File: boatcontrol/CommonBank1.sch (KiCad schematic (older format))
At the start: 24 parts, among them J201 Conn_01x01_Male, J202 Conn_01x01_Male, J203 TBP01R2W-508-16BE, J204 Conn_01x01_Male, J205 Conn_01x01_Male, J206 TBL008V-1000-02BE, Q203 IPP120P04P4L-03, U201 MCP23017-E/SP, U202 MCP23017-E/SP

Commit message: RPi scheme update done
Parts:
- JP209: value Jumper_NO_Small -> Jumper_NC_Small; symbol Device:Jumper_NO_Small -> Device:Jumper_NC_Small
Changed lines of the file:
@@
 	8500 5550 8500 5750
 $Comp
-L Device:Jumper_NO_Small JP?
+L Device:Jumper_NC_Small JP?
 U 1 1 617F409D
 P 9800 5800
@@
 AR Path="/D1BB8DB4/617F409D" Ref="JP?"  Part="1"
 F 0 "JP209" H 9800 5900 50  0000 C CNN
-F 1 "Jumper_NO_Small" H 9850 5700 50  0001 C CNN
+F 1 "Jumper_NC_Small" H 9850 5700 50  0001 C CNN
 F 2 "Connector_PinHeader_2.54mm:PinHeader_1x02_P2.54mm_Vertical" H 9800 5800 50  0001 C CNN
 F 3 "~" H 9800 5800 50  0001 C CNN

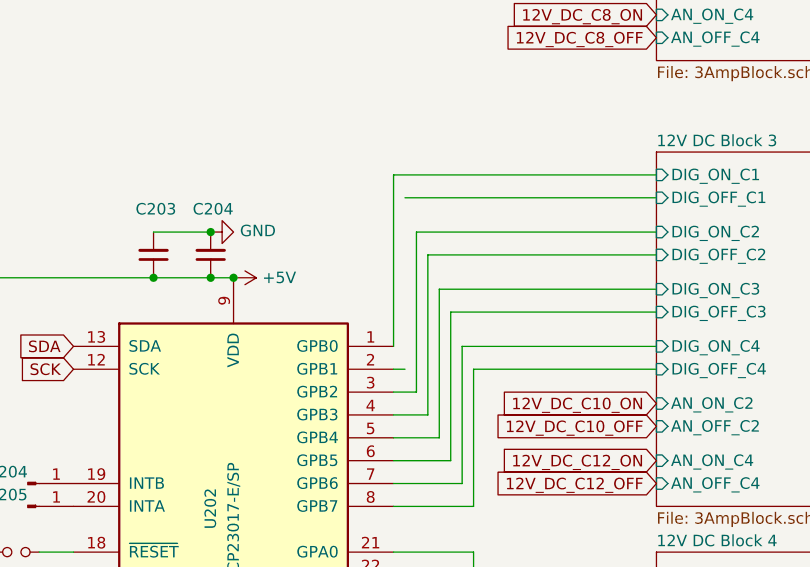
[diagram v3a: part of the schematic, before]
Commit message: Line up jumpers
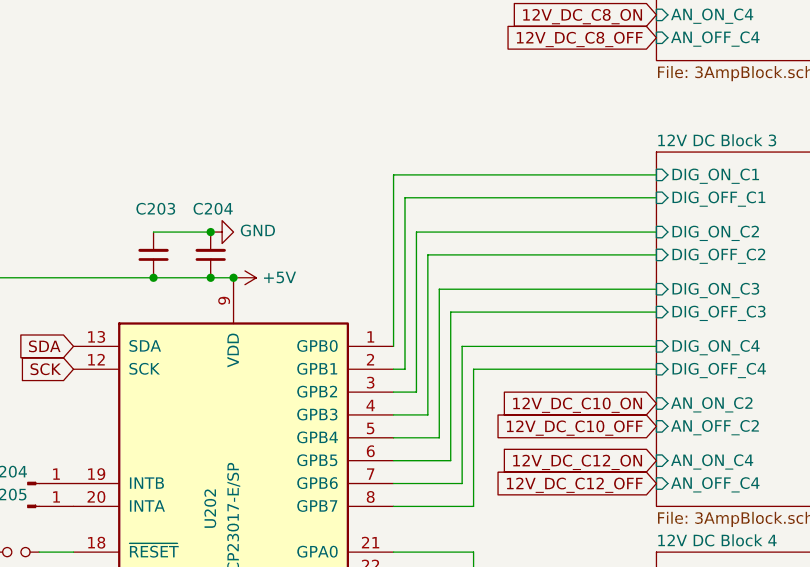
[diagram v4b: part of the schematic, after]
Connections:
- net 12V DC Block 3/DIG_OFF_C1: now also U202.2 (GPB1)
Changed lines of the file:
@@
 	-1   0    0    1
 $EndComp
+Wire Wire Line
+	4300 5350 4300 4600
 $EndSCHEMATC

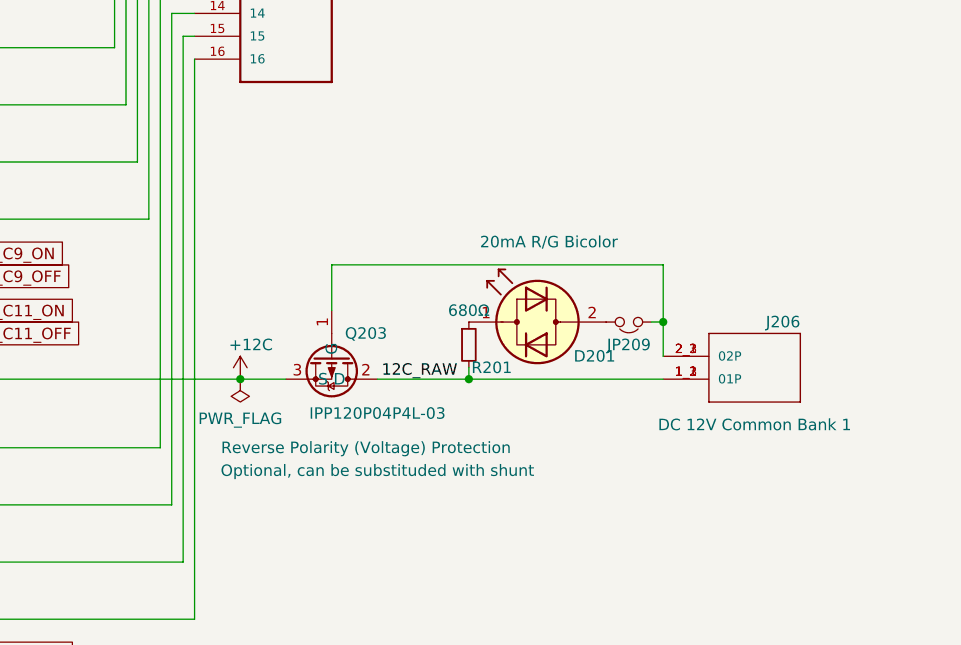
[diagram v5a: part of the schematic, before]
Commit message: Scale reverse polarity protection
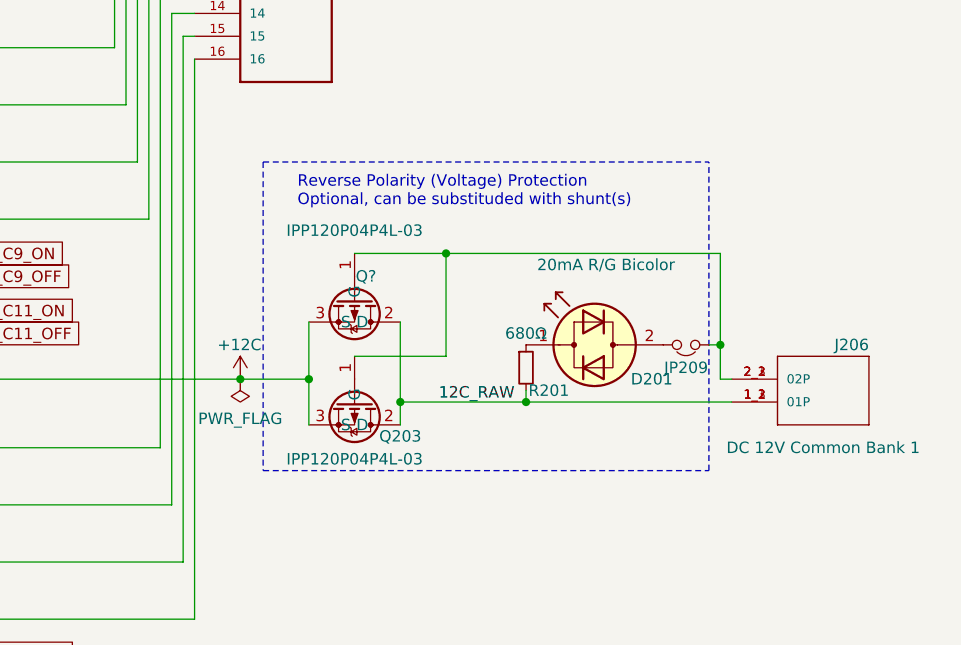
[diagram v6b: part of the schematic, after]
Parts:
- added Q?: IPP120P04P4L-03, Package_TO_SOT_THT:TO-220-3_Vertical, symbol BoatControl:IPP120P04P4L-03
- Q203: Field8 Optional, can be substituded with shunt -> (none); Purpose Reverse Polarity (Voltage) Protection -> (none)
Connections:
- net +12C: now also Q?.3 (S)
- net 12C_RAW: now also Q?.2 (D)
- net at J206.2_1 (02P), J206.2_2 (02P), J206.2_3 (02P)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: now also Q?.1 (G)
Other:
- note added: "Reverse Polarity (Voltage) Protection\nOptional, can be substituded with shunt(s)"
- moved on the sheet: D201, J206, JP209, Q203, R201
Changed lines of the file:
@@
 AR Path="/D1BB8DB4/D1AAA2AE" Ref="#PWR?"  Part="1"
 F 0 "#PWR0205" H 8100 5900 50  0001 C CNN
-F 1 "+12C" H 8050 6200 50  0000 L CNN
+F 1 "+12C" H 8000 6200 50  0000 L CNN
 F 2 "" H 8100 6050 50  0001 C CNN
 F 3 "" H 8100 6050 50  0001 C CNN
@@
 Wire Wire Line
 	6750 5250 6750 6050
-Wire Wire Line
-	8300 6050 8100 6050
 Connection ~ 6750 6050
 Wire Wire Line
@@
 Wire Wire Line
 	4600 1650 5400 1650
-Text Label 9050 6050 2    50   ~ 0
+Text Label 9300 6150 2    50   ~ 0
 12C_RAW
 Connection ~ 8100 6050
@@
 L BoatControl:TBL008V-1000-02BE J?
 U 1 1 D1AAA18D
-P 10350 5950
+P 10650 6050
 AR Path="/D1AAA18D" Ref="J?"  Part="1"
 AR Path="/D16552B4/D1AAA18D" Ref="J206"  Part="1"
 AR Path="/D1BB8DB4/D1AAA18D" Ref="J?"  Part="1"
-F 0 "J206" H 10550 5800 50  0000 R CNN
-F 1 "TBL008V-1000-02BE" H 10700 5800 50  0001 R CNN
-F 2 "CUI_TBL008V-1000-02BE" H 10350 5950 50  0001 L BNN
-F 3 "CUI" H 10350 5950 50  0001 L BNN
-F 4 "DC 12V Common Bank 1" H 10350 6250 50  0000 C CNN "Type"
-	1    10350 5950
+F 0 "J206" H 10850 5900 50  0000 R CNN
+F 1 "TBL008V-1000-02BE" H 11000 5900 50  0001 R CNN
+F 2 "CUI_TBL008V-1000-02BE" H 10650 6050 50  0001 L BNN
+F 3 "CUI" H 10650 6050 50  0001 L BNN
+F 4 "DC 12V Common Bank 1" H 10650 6350 50  0000 C CNN "Type"
+	1    10650 6050
 	1    0    0    1
 $EndComp
@@
 L BoatControl:IPP120P04P4L-03 Q203
 U 1 1 5FEBFE7C
-P 8500 6050
-F 0 "Q203" V 8300 6200 50  0000 C CNN
-F 1 "IPP120P04P4L-03" V 8650 6250 50  0000 C CNN
-F 2 "Package_TO_SOT_THT:TO-220-3_Vertical" H 8150 6600 50  0001 C CNN
-F 3 "https://www.infineon.com/dgdl/Infineon-I80P03P4L_04-DS-v01_01-en.pdf?folderId=db3a304314dca3890114ef902baa05f9&fileId=db3a30431ddc9372011e07e95eb827d7&ack=t" H 8500 6050 50  0001 C CNN
-F 4 "P-Channel 30V 80A (Tc) 137W (Tc) Through Hole PG-TO220-3-1" H 8350 6700 50  0001 C CNN "Description"
-F 5 "OptiMOS" H 9100 6350 50  0001 C CNN "Series"
-F 6 "Infineon Technologies" H 9000 6450 50  0001 C CNN "Infineon Technologies"
-F 7 "Reverse Polarity (Voltage) Protection" V 8800 6200 50  0000 C CNN "Purpose"
-F 8 "Optional, can be substituded with shunt" V 8900 6250 50  0000 C CNN "Field8"
-	1    8500 6050
+P 8600 6250
+F 0 "Q203" V 8650 6450 50  0000 C CNN
+F 1 "IPP120P04P4L-03" V 8750 6250 50  0000 C CNN
+F 2 "Package_TO_SOT_THT:TO-220-3_Vertical" H 8250 6800 50  0001 C CNN
+F 3 "https://www.infineon.com/dgdl/Infineon-I80P03P4L_04-DS-v01_01-en.pdf?folderId=db3a304314dca3890114ef902baa05f9&fileId=db3a30431ddc9372011e07e95eb827d7&ack=t" H 8600 6250 50  0001 C CNN
+F 4 "P-Channel 30V 80A (Tc) 137W (Tc) Through Hole PG-TO220-3-1" H 8450 6900 50  0001 C CNN "Description"
+F 5 "OptiMOS" H 9200 6550 50  0001 C CNN "Series"
+F 6 "Infineon Technologies" H 9100 6650 50  0001 C CNN "Infineon Technologies"
+	1    8600 6250
 	0    1    1    0
 $EndComp
@@
 L Device:LED_Dual_2pin D?
 U 1 1 5FECB36F
-P 9400 5800
+P 9650 5900
 AR Path="/5FECB36F" Ref="D?"  Part="1"
 AR Path="/5FBFBEC9/5FECB36F" Ref="D?"  Part="1"
@@
 AR Path="/D1BB8DB4/5F75E923/60474911/5FECB36F" Ref="D?"  Part="1"
 AR Path="/D16552B4/5FECB36F" Ref="D201"  Part="1"
-F 0 "D201" H 9150 5650 50  0000 C CNN
-F 1 "20mA R/G Bicolor" H 9350 6150 50  0000 C CNN
-F 2 "LED_THT:LED_D5.0mm" H 9400 5800 50  0001 C CNN
-F 3 "http://www.kingbrightusa.com/images/catalog/SPEC/WP59EGW-CA.pdf" H 9400 5800 50  0001 C CNN
-F 4 "WP57EGW" H 9400 5800 50  0001 C CNN "Model"
-F 5 "Kingbright" H 9400 5800 50  0001 C CNN "Manufacturer"
-	1    9400 5800
+F 0 "D201" H 9400 5750 50  0000 C CNN
+F 1 "20mA R/G Bicolor" H 9600 6250 50  0000 C CNN
+F 2 "LED_THT:LED_D5.0mm" H 9650 5900 50  0001 C CNN
+F 3 "http://www.kingbrightusa.com/images/catalog/SPEC/WP59EGW-CA.pdf" H 9650 5900 50  0001 C CNN
+F 4 "WP57EGW" H 9650 5900 50  0001 C CNN "Model"
+F 5 "Kingbright" H 9650 5900 50  0001 C CNN "Manufacturer"
+	1    9650 5900
 	-1   0    0    -1
 $EndComp
@@
 L Device:R_Small R201
 U 1 1 5FE96CCA
-P 9100 5900
-F 0 "R201" H 9200 5800 50  0000 C CNN
-F 1 "680Ω" H 9100 6050 50  0000 C CNN
-F 2 "Resistor_THT:R_Axial_DIN0207_L6.3mm_D2.5mm_P7.62mm_Horizontal" H 9100 5900 50  0001 C CNN
-F 3 "https://www.te.com/commerce/DocumentDelivery/DDEController?Action=srchrtrv&DocNm=1773241&DocType=DS&DocLang=English" H 9100 5900 50  0001 C CNN
-F 4 "LR1F680R" H 9100 5900 50  0001 C CNN "Product"
-F 5 "TE Connectivity" H 9100 5900 50  0001 C CNN "Manufacturer"
-F 6 "680 Ohms ±1% 0.6W Through Hole Resistor Axial Metal Film" H 9100 5900 50  0001 C CNN "Description"
-	1    9100 5900
+P 9350 6000
+F 0 "R201" H 9450 5900 50  0000 C CNN
+F 1 "680Ω" H 9350 6150 50  0000 C CNN
+F 2 "Resistor_THT:R_Axial_DIN0207_L6.3mm_D2.5mm_P7.62mm_Horizontal" H 9350 6000 50  0001 C CNN
+F 3 "https://www.te.com/commerce/DocumentDelivery/DDEController?Action=srchrtrv&DocNm=1773241&DocType=DS&DocLang=English" H 9350 6000 50  0001 C CNN
+F 4 "LR1F680R" H 9350 6000 50  0001 C CNN "Product"
+F 5 "TE Connectivity" H 9350 6000 50  0001 C CNN "Manufacturer"
+F 6 "680 Ohms ±1% 0.6W Through Hole Resistor Axial Metal Film" H 9350 6000 50  0001 C CNN "Description"
+	1    9350 6000
 	1    0    0    -1
 $EndComp
 Wire Wire Line
-	8700 6050 9100 6050
-Wire Wire Line
-	9100 6000 9100 6050
-Connection ~ 9100 6050
-Wire Wire Line
-	9100 6050 9950 6050
-Wire Wire Line
-	9950 5550 8500 5550
-Wire Wire Line
-	8500 5550 8500 5750
+	9350 6100 9350 6150
 $Comp
 L Device:Jumper_NC_Small JP?
 U 1 1 617F409D
-P 9800 5800
+P 10050 5900
 AR Path="/617F409D" Ref="JP?"  Part="1"
 AR Path="/D16552B4/617F409D" Ref="JP209"  Part="1"
 AR Path="/D1BB8DB4/617F409D" Ref="JP?"  Part="1"
-F 0 "JP209" H 9800 5900 50  0000 C CNN
-F 1 "Jumper_NC_Small" H 9850 5700 50  0001 C CNN
-F 2 "Connector_PinHeader_2.54mm:PinHeader_1x02_P2.54mm_Vertical" H 9800 5800 50  0001 C CNN
-F 3 "~" H 9800 5800 50  0001 C CNN
-	1    9800 5800
+F 0 "JP209" H 10050 6000 50  0000 C CNN
+F 1 "Jumper_NC_Small" H 10100 5800 50  0001 C CNN
+F 2 "Connector_PinHeader_2.54mm:PinHeader_1x02_P2.54mm_Vertical" H 10050 5900 50  0001 C CNN
+F 3 "~" H 10050 5900 50  0001 C CNN
+	1    10050 5900
 	-1   0    0    1
 $EndComp
 Wire Wire Line
-	9950 5550 9950 5800
-Wire Wire Line
-	9900 5800 9950 5800
-Connection ~ 9950 5800
-Wire Wire Line
-	9950 5800 9950 5950
+	10150 5900 10200 5900
 Wire Wire Line
 	3200 600  3450 600
@@
 Wire Wire Line
 	4300 5350 4300 4600
+$Comp
+L BoatControl:IPP120P04P4L-03 Q?
+U 1 1 63B17605
+P 8600 5800
+F 0 "Q?" V 8400 5850 50  0000 C CNN
+F 1 "IPP120P04P4L-03" V 8200 5800 50  0000 C CNN
+F 2 "Package_TO_SOT_THT:TO-220-3_Vertical" H 8250 6350 50  0001 C CNN
+F 3 "https://www.infineon.com/dgdl/Infineon-I80P03P4L_04-DS-v01_01-en.pdf?folderId=db3a304314dca3890114ef902baa05f9&fileId=db3a30431ddc9372011e07e95eb827d7&ack=t" H 8600 5800 50  0001 C CNN
+F 4 "P-Channel 30V 80A (Tc) 137W (Tc) Through Hole PG-TO220-3-1" H 8450 6450 50  0001 C CNN "Description"
+F 5 "OptiMOS" H 9200 6100 50  0001 C CNN "Series"
+F 6 "Infineon Technologies" H 9100 6200 50  0001 C CNN "Infineon Technologies"
+	1    8600 5800
+	0    1    1    0
+$EndComp
+Text Notes 8350 5300 0    50   ~ 0
+Reverse Polarity (Voltage) Protection\nOptional, can be substituded with shunt(s)
+Wire Wire Line
+	9350 6150 10250 6150
+Wire Wire Line
+	10200 5900 10200 6050
+Wire Wire Line
+	10250 6050 10200 6050
+Wire Wire Line
+	8600 5500 9000 5500
+Wire Wire Line
+	10200 5500 10200 5900
+Connection ~ 10200 5900
+Wire Wire Line
+	8600 5950 9000 5950
+Wire Wire Line
+	9000 5950 9000 5500
+Connection ~ 9000 5500
+Wire Wire Line
+	9000 5500 10200 5500
+Wire Wire Line
+	8800 5800 8800 6150
+Wire Wire Line
+	9350 6150 8800 6150
+Connection ~ 9350 6150
+Connection ~ 8800 6150
+Wire Wire Line
+	8800 6150 8800 6250
+Wire Wire Line
+	8400 5800 8400 6050
+Wire Wire Line
+	8100 6050 8400 6050
+Connection ~ 8400 6050
+Wire Wire Line
+	8400 6050 8400 6250
+Wire Notes Line
+	8200 5100 8200 6450
+Wire Notes Line
+	8200 6450 10150 6450
+Wire Notes Line
+	10150 6450 10150 5100
+Wire Notes Line
+	8200 5100 10150 5100
 $EndSCHEMATC

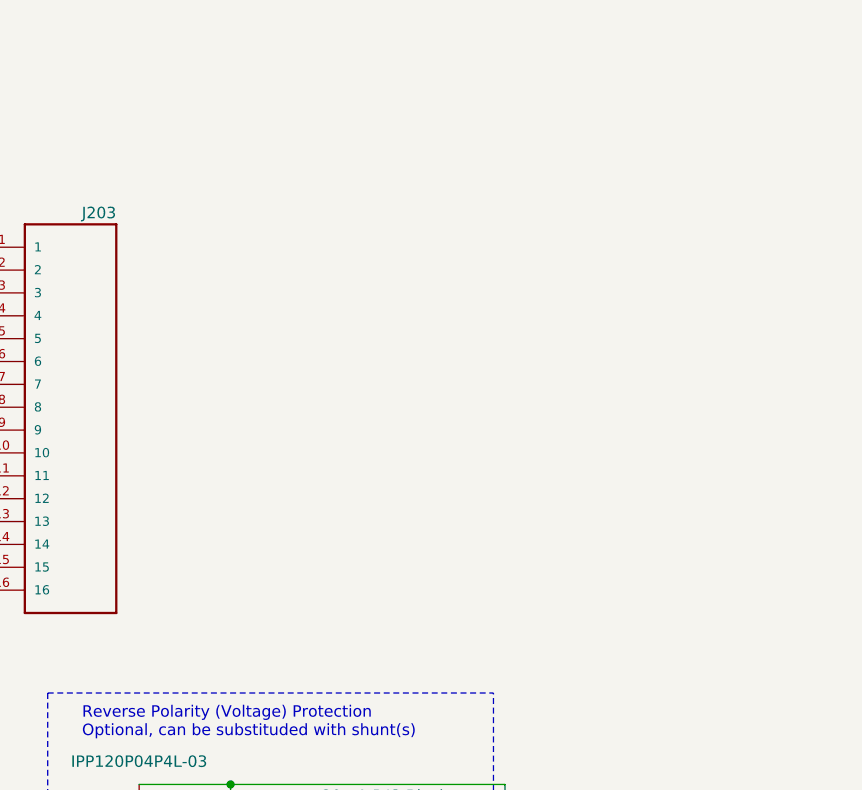
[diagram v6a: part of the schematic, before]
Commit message: Add notes about power use of polarity protection
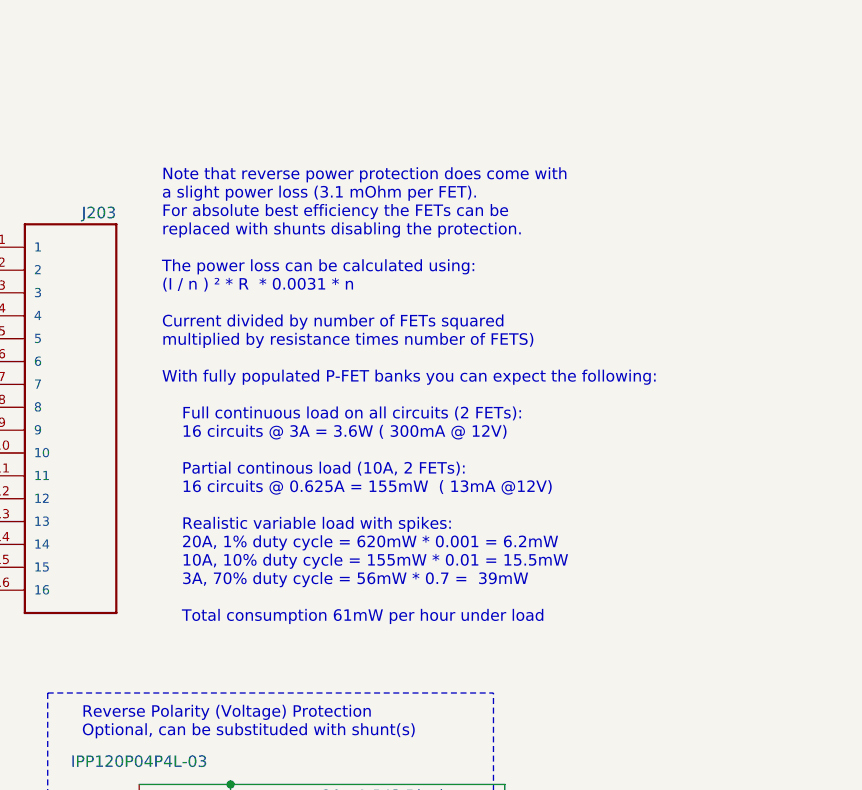
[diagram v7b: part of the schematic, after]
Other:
- note added: "Note that reverse power protection does come with\na slight power loss (3.1 mOhm per FET).\nFor absolute best efficiency the FETs can be\nreplaced with shunts disabling the protection.\n\nThe power loss can be calculated using:\n(I / n ) ² * R * 0.0031 * n\n\nCurrent divided by number of FETs squared\nmultiplied by resistance times number of FETS) \n\nWith fully populated P-FET banks you can expe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"
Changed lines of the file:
@@
 $Descr A4 11693 8268
 encoding utf-8
-Sheet 13 97
+Sheet 2 97
 Title "Boat Control Hat"
 Date "2020-07-09"
@@
 Wire Notes Line
 	8200 5100 10150 5100
+Text Notes 8700 4800 0    50   ~ 0
+Note that reverse power protection does come with\na slight power loss (3.1 mOhm per FET).\nFor absolute best efficiency the FETs can be\nreplaced with shunts disabling the protection.\n\nThe power loss can be calculated using:\n(I / n ) ² * R  * 0.0031 * n\n\nCurrent divided by number of FETs squared\nmultiplied by resistance times number of FETS) \n\nWith fully populated P-FET banks you can expect the following:\n\n    Full continuous load on all circuits (2 FETs):\n    16 circuits @ 3A = 3.6W ( 300mA @ 12V)\n\n    Partial continous load (10A, 2 FETs):\n    16 circuits @ 0.625A = 155mW  ( 13mA @12V)\n\n    Realistic variable load with spikes:\n    20A, 1% duty cycle = 620mW * 0.001 = 6.2mW\n    10A, 10% duty cycle = 155mW * 0.01 = 15.5mW\n    3A, 70% duty cycle = 56mW * 0.7 =  39mW\n    \n    Total consumption 61mW per hour under load\n
 $EndSCHEMATC

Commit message: Cleanup
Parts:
- D201: symbol Device:LED_Dual_2pin -> boatcontrol-rescue:LED_Dual_2pin-Device
- JP201, JP205: symbol Device:Jumper_NO_Small -> boatcontrol-rescue:Jumper_NO_Small-Device
- JP202, JP203, JP204, JP206, JP207, JP208: symbol Jumper:SolderJumper_3_Bridged12_Output -> boatcontrol-rescue:SolderJumper_3_Bridged12_Output-Jumper
- JP209: symbol Device:Jumper_NC_Small -> boatcontrol-rescue:Jumper_NC_Small-Device
- gave numbers to parts that had none: 1
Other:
- moved on the sheet: C201, C202, C203, C204, D201, J201, J202, J203, J204, J205, J206, JP201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
